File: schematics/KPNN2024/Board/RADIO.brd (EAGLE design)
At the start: 68.2 x 68.2 mm, 16 parts, among them J1 IPX-RADIO, J2 IPX-ANT

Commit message: ййййййййййййййййййййййййййййййййййй
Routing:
- net GND: track 161.2 -> 160.4 mm
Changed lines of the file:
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@@
 <?xml version="1.0" encoding="utf-8"?>
 <!DOCTYPE eagle SYSTEM "eagle.dtd">
-<eagle version="9.4.2">
+<eagle version="9.6.2">
 <drawing>
 <settings>
-<setting alwaysvectorfont="yes"/>
+<setting alwaysvectorfont="no"/>
 <setting verticaltext="up"/>
 </settings>
@@
 <contactref element="ROTATE2" pad="3"/>
 <contactref element="ROTATE1" pad="3"/>
-<wire x1="68.3698" y1="43.68434375" x2="68.477071875" y2="43.577071875" width="0.3" layer="1"/>
 <wire x1="64.921015625" y1="48.18434375" x2="64.985015625" y2="48.12034375" width="0.3" layer="1"/>
 <wire x1="64.985015625" y1="48.12034375" x2="64.985015625" y2="46.04934375" width="0.3" layer="1"/>
@@
 <wire x1="49.1" y1="48.18434375" x2="64.921015625" y2="48.18434375" width="0.5" layer="1"/>
 <wire x1="64.921015625" y1="48.18434375" x2="64.921015625" y2="43.68434375" width="0.5" layer="1"/>
-<wire x1="64.921015625" y1="43.68434375" x2="68.3698" y2="43.68434375" width="0.5" layer="1"/>
-<wire x1="68.477071875" y1="43.577071875" x2="68.636471875" y2="43.417671875" width="0.5" layer="1"/>
-<wire x1="68.636471875" y1="43.417671875" x2="68.636471875" y2="42.617671875" width="0.5" layer="1"/>
 <wire x1="68.636471875" y1="42.617671875" x2="68.636471875" y2="39.667671875" width="0.5" layer="1"/>
-<wire x1="68.636471875" y1="39.667671875" x2="68.15314375" y2="39.18434375" width="0.5" layer="1"/>
-<wire x1="68.15314375" y1="39.18434375" x2="64.921015625" y2="39.18434375" width="0.5" layer="1"/>
 <wire x1="24.741128125" y1="33.09638125" x2="24.741128125" y2="36.38238125" width="0.5" layer="1"/>
 <wire x1="24.734015625" y1="43.71034375" x2="23.034015625" y2="43.71034375" width="0.5" layer="1"/>
@@
 <wire x1="23.541128125" y1="36.38238125" x2="24.741128125" y2="36.38238125" width="0.5" layer="1"/>
 <wire x1="24.734015625" y1="43.71034375" x2="24.734015625" y2="46.66034375" width="0.5" layer="1"/>
-<wire x1="24.734015625" y1="46.66034375" x2="25.258015625" y2="47.18434375" width="0.5" layer="1"/>
-<wire x1="25.258015625" y1="47.18434375" x2="28.521015625" y2="47.18434375" width="0.5" layer="1"/>
-<wire x1="24.734015625" y1="43.71034375" x2="24.734015625" y2="43.18434375" width="0.5" layer="1"/>
-<wire x1="24.734015625" y1="43.18434375" x2="28.521015625" y2="43.18434375" width="0.5" layer="1"/>
 <wire x1="64.921015625" y1="48.18434375" x2="66.05634375" y2="48.18434375" width="0.5" layer="1"/>
 <wire x1="66.05634375" y1="48.18434375" x2="66.12034375" y2="48.12034375" width="0.5" layer="1"/>
@@
 <wire x1="69.23434375" y1="30.18434375" x2="64.921015625" y2="30.18434375" width="0.5" layer="1"/>
 <wire x1="61.8" y1="29.2" x2="62.8" y2="30.2" width="0.5" layer="1"/>
+<wire x1="68.636471875" y1="39.667671875" x2="68.15314375" y2="39.18434375" width="1" layer="1"/>
+<wire x1="68.15314375" y1="39.18434375" x2="64.921015625" y2="39.18434375" width="1" layer="1"/>
+<wire x1="68.636471875" y1="42.617671875" x2="67.5698" y2="43.68434375" width="1" layer="1"/>
+<wire x1="67.5698" y1="43.68434375" x2="64.921015625" y2="43.68434375" width="1" layer="1"/>
+<wire x1="24.734015625" y1="43.71034375" x2="25.260015625" y2="43.18434375" width="1" layer="1"/>
+<wire x1="25.260015625" y1="43.18434375" x2="28.521015625" y2="43.18434375" width="1" layer="1"/>
+<wire x1="24.734015625" y1="46.66034375" x2="25.258015625" y2="47.18434375" width="1" layer="1"/>
+<wire x1="25.258015625" y1="47.18434375" x2="28.521015625" y2="47.18434375" width="1" layer="1"/>
 </signal>
 <signal name="3V3">
@@
 <contactref element="J1" pad="3"/>
 <contactref element="XQ-02A" pad="RF-IN"/>
-<wire x1="67.111471875" y1="41.142671875" x2="64.9626875" y2="41.142671875" width="0.3" layer="1"/>
-<wire x1="64.921015625" y1="41.18434375" x2="64.9626875" y2="41.142671875" width="0.3" layer="1"/>
+<wire x1="67.111471875" y1="41.142671875" x2="64.9626875" y2="41.142671875" width="0.75" layer="1"/>
+<wire x1="64.9626875" y1="41.142671875" x2="64.921015625" y2="41.18434375" width="0.75" layer="1"/>
 </signal>
 <signal name="ANT_RADIO">
 <contactref element="J2" pad="3"/>
 <contactref element="XQ-02A" pad="ANT"/>
-<wire x1="26.259015625" y1="45.18534375" x2="28.520015625" y2="45.18534375" width="0.3" layer="1"/>
-<wire x1="28.520015625" y1="45.18534375" x2="28.521015625" y2="45.18434375" width="0.3" layer="1"/>
+<wire x1="26.259015625" y1="45.18534375" x2="28.520015625" y2="45.18534375" width="0.75" layer="1"/>
+<wire x1="28.520015625" y1="45.18534375" x2="28.521015625" y2="45.18434375" width="0.75" layer="1"/>
 </signal>
 <signal name="DIR_DRIVER">

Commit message: сдклвл платы а мботрен зз
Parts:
- moved NRF24LO1 0.37 mm to (50.0, 69.0)
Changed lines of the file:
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@@
 <attribute name="VALUE" x="24.5599875" y="48.321015625" size="1" layer="27" font="vector" ratio="15" align="center"/>
 </element>
-<element name="GPS-NEO7M" library="UNKNOWN-2024" package="GPS-NEO7M" value="GPS-NEO7M" x="50.900509375" y="64.0324625" smashed="yes" rot="MR270">
-<attribute name="NAME" x="61.5324625" y="77.099490625" size="1" layer="28" font="vector" ratio="15" rot="MR0"/>
-</element>
-<element name="NRF24LO1" library="UNKNOWN-2024" package="NRF24L01_ML01SP4" value="NRF24L01_ML01SP4" x="50.36748125" y="69.018953125" smashed="yes">
-<attribute name="NAME" x="41.36748125" y="77.118953125" size="1" layer="25" font="vector" ratio="15"/>
+<element name="GPS-NEO7M" library="UNKNOWN-2024" package="GPS-NEO7M" value="GPS-NEO7M" x="50.9" y="64" smashed="yes" rot="MR270">
+<attribute name="NAME" x="61.531953125" y="77.067028125" size="1" layer="28" font="vector" ratio="15" rot="MR0"/>
+</element>
+<element name="NRF24LO1" library="UNKNOWN-2024" package="NRF24L01_ML01SP4" value="NRF24L01_ML01SP4" x="50" y="69" smashed="yes">
+<attribute name="NAME" x="41" y="77.1" size="1" layer="25" font="vector" ratio="15"/>
 </element>
 <element name="XQ-02A" library="UNKNOWN-2024" package="XQ-02A" value="XQ-02A" x="46.721015625" y="37.18434375" smashed="yes" rot="R180">
@@
 <wire x1="29.714175" y1="47.18434375" x2="31.15" y2="48.62016875" width="0.5" layer="1"/>
 <wire x1="31.15" y1="56.4" x2="31.15" y2="48.62016875" width="0.5" layer="1"/>
-<wire x1="34.900509375" y1="60.2224625" x2="34.900509375" y2="60.150509375" width="0.5" layer="1"/>
+<wire x1="34.9" y1="60.19" x2="34.900509375" y2="60.150509375" width="0.5" layer="1"/>
 <wire x1="34.900509375" y1="60.150509375" x2="31.15" y2="56.4" width="0.5" layer="1"/>
-<wire x1="34.900509375" y1="60.2224625" x2="39.252" y2="64.573953125" width="0.5" layer="1"/>
-<wire x1="39.252" y1="64.573953125" x2="41.36748125" y2="64.573953125" width="0.5" layer="1"/>
-<wire x1="41.36748125" y1="64.573953125" x2="41.36748125" y2="55.9168625" width="0.5" layer="1"/>
-<wire x1="41.36748125" y1="55.9168625" x2="49.1" y2="48.18434375" width="0.5" layer="1"/>
+<wire x1="41" y1="56.28434375" x2="49.1" y2="48.18434375" width="0.5" layer="1"/>
 <wire x1="49.1" y1="48.18434375" x2="64.921015625" y2="48.18434375" width="0.5" layer="1"/>
 <wire x1="64.921015625" y1="48.18434375" x2="64.921015625" y2="43.68434375" width="0.5" layer="1"/>
@@
 <wire x1="24.734015625" y1="46.66034375" x2="25.258015625" y2="47.18434375" width="1" layer="1"/>
 <wire x1="25.258015625" y1="47.18434375" x2="28.521015625" y2="47.18434375" width="1" layer="1"/>
+<wire x1="41" y1="64.555" x2="41" y2="56.28434375" width="0.5" layer="1"/>
+<wire x1="34.9" y1="60.19" x2="39.265" y2="64.555" width="0.5" layer="1"/>
+<wire x1="39.265" y1="64.555" x2="41" y2="64.555" width="0.5" layer="1"/>
 </signal>
 <signal name="3V3">
@@
 <wire x1="31.08238125" y1="36.38238125" x2="37.7" y2="42.9" width="0.5" layer="1"/>
 <via x="37.7" y="42.9" extent="1-16" drill="0.35"/>
-<wire x1="41.36748125" y1="73.463953125" x2="37.736046875" y2="73.463953125" width="0.5" layer="1"/>
+<wire x1="41" y1="73.445" x2="37.736046875" y2="73.463953125" width="0.5" layer="1"/>
 <wire x1="37.736046875" y1="73.463953125" x2="37.7" y2="73.5" width="0.5" layer="1"/>
 <wire x1="37.7" y1="73.5" x2="37.7" y2="73.45" width="0.5" layer="1"/>
 <via x="37.7" y="73.45" extent="1-16" drill="0.35"/>
-<wire x1="41.36748125" y1="73.463953125" x2="43.476046875" y2="73.463953125" width="0.5" layer="1"/>
+<wire x1="41" y1="73.445" x2="43.476046875" y2="73.463953125" width="0.5" layer="1"/>
 <wire x1="43.476046875" y1="73.463953125" x2="49.7" y2="67.24" width="0.5" layer="1"/>
 <wire x1="71.16" y1="67.24" x2="71.2" y2="67.2" width="0.5" layer="1"/>
@@
 <wire x1="37.7" y1="42.9" x2="37.7" y2="67.8" width="0.5" layer="16"/>
 <wire x1="37.7" y1="67.8" x2="37.7" y2="73.45" width="0.5" layer="16"/>
-<wire x1="34.900509375" y1="67.8424625" x2="37.6575375" y2="67.8424625" width="0.5" layer="16"/>
-<wire x1="37.6575375" y1="67.8424625" x2="37.7" y2="67.8" width="0.5" layer="16"/>
+<wire x1="34.9" y1="67.81" x2="37.69" y2="67.81" width="0.5" layer="16"/>
+<wire x1="37.69" y1="67.81" x2="37.7" y2="67.8" width="0.5" layer="16"/>
 </signal>
 <signal name="5V">
@@
 <contactref element="NRF24LO1" pad="P$2"/>
 <wire x1="28.35" y1="72.16" x2="41.333528125" y2="72.16" width="0.3" layer="1"/>
-<wire x1="41.333528125" y1="72.16" x2="41.36748125" y2="72.193953125" width="0.3" layer="1"/>
+<wire x1="41.333528125" y1="72.16" x2="41" y2="72.175" width="0.3" layer="1"/>
 </signal>
 <signal name="CS_RADIO">
@@
 <contactref element="NRF24LO1" pad="P$3"/>
 <wire x1="25.65" y1="69.62" x2="25.65" y2="70.45" width="0.3" layer="1"/>
-<wire x1="25.65" y1="70.45" x2="26.123953125" y2="70.923953125" width="0.3" layer="1"/>
-<wire x1="26.123953125" y1="70.923953125" x2="33.4" y2="70.923953125" width="0.3" layer="1"/>
-<wire x1="33.4" y1="70.923953125" x2="41.36748125" y2="70.923953125" width="0.3" layer="1"/>
+<wire x1="25.65" y1="70.45" x2="26.105" y2="70.905" width="0.3" layer="1"/>
+<wire x1="26.105" y1="70.905" x2="41" y2="70.905" width="0.3" layer="1"/>
 </signal>
 <signal name="IRQ_RADIO">
 <contactref element="U$7" pad="3"/>
 <contactref element="NRF24LO1" pad="P$7"/>
-<wire x1="41.36748125" y1="65.843953125" x2="41.23090625" y2="65.980528125" width="0.3" layer="1"/>
-<wire x1="41.23090625" y1="65.980528125" x2="38.619471875" y2="65.980528125" width="0.3" layer="1"/>
-<wire x1="38.619471875" y1="65.980528125" x2="38.6" y2="66" width="0.3" layer="1"/>
 <via x="38.6" y="66" extent="1-16" drill="0.35"/>
 <wire x1="38.6" y1="75.10326875" x2="38.6" y2="66" width="0.3" layer="16"/>
@@
 <wire x1="38.6" y1="75.10326875" x2="36.30480625" y2="77.3984625" width="0.3" layer="16"/>
 <wire x1="33.3984625" y1="77.3984625" x2="31.2006375" y2="75.2006375" width="0.3" layer="16"/>
+<wire x1="38.6" y1="66" x2="38.775" y2="65.825" width="0.3" layer="1"/>
+<wire x1="38.775" y1="65.825" x2="41" y2="65.825" width="0.3" layer="1"/>
 </signal>
 <signal name="MOSI_RADIO">
 <contactref element="U$7" pad="4"/>
 <contactref element="NRF24LO1" pad="P$5"/>
-<wire x1="41.36748125" y1="68.383953125" x2="39.116046875" y2="68.383953125" width="0.3" layer="1"/>
-<wire x1="39.116046875" y1="68.383953125" x2="38.3" y2="69.2" width="0.3" layer="1"/>
-<wire x1="38.3" y1="69.2" x2="29" y2="69.2" width="0.3" layer="1"/>
+<wire x1="29" y1="69.2" x2="38.3" y2="69.2" width="0.3" layer="1"/>
 <wire x1="24.8071125" y1="68.1" x2="23.50355625" y2="66.79644375" width="0.3" layer="1"/>
 <wire x1="23.50355625" y1="66.79644375" x2="23.50355625" y2="64.89644375" width="0.3" layer="1"/>
@@
 <wire x1="29" y1="69.2" x2="27.9" y2="68.1" width="0.3" layer="1"/>
 <wire x1="27.9" y1="68.1" x2="24.8071125" y2="68.1" width="0.3" layer="1"/>
+<wire x1="39.135" y1="68.365" x2="41" y2="68.365" width="0.3" layer="1"/>
+<wire x1="38.3" y1="69.2" x2="39.135" y2="68.365" width="0.3" layer="1"/>
 </signal>
 <signal name="MISO_RADIO">
@@
 <wire x1="30.35" y1="62.3" x2="30.05" y2="62" width="0.3" layer="1"/>
 <wire x1="28.35" y1="62" x2="30.05" y2="62" width="0.3" layer="1"/>
-<wire x1="41.36748125" y1="67.113953125" x2="41.253528125" y2="67" width="0.3" layer="1"/>
-<wire x1="41.253528125" y1="67" x2="39.4" y2="67" width="0.3" layer="1"/>
 <via x="39.4" y="67" extent="1-16" drill="0.35"/>
 <wire x1="39.4" y1="76.6" x2="39.4" y2="67" width="0.3" layer="16"/>
@@
 <wire x1="39.4" y1="76.6" x2="37.6015375" y2="78.3984625" width="0.3" layer="16"/>
 <wire x1="33.3984625" y1="78.3984625" x2="30.3" y2="75.3" width="0.3" layer="16"/>
+<wire x1="39.4" y1="67" x2="40.905" y2="67" width="0.3" layer="1"/>
+<wire x1="40.905" y1="67" x2="41" y2="67.095" width="0.3" layer="1"/>
 </signal>
 <signal name="SCK_RADIO">
@@
 <wire x1="23.84" y1="59.46" x2="23" y2="60.3" width="0.3" layer="1"/>
 <wire x1="23" y1="67" x2="23" y2="60.3" width="0.3" layer="1"/>
-<wire x1="41.36748125" y1="69.653953125" x2="39.06748125" y2="69.653953125" width="0.3" layer="1"/>
-<wire x1="39.06748125" y1="69.653953125" x2="38.66748125" y2="70.053953125" width="0.3" layer="1"/>
-<wire x1="38.66748125" y1="70.053953125" x2="29.053953125" y2="70.053953125" width="0.3" layer="1"/>
+<wire x1="29.053953125" y1="70.053953125" x2="38.66748125" y2="70.053953125" width="0.3" layer="1"/>
 <wire x1="29.053953125" y1="70.053953125" x2="27.6" y2="68.6" width="0.3" layer="1"/>
 <wire x1="27.6" y1="68.6" x2="24.6" y2="68.6" width="0.3" layer="1"/>
 <wire x1="24.6" y1="68.6" x2="23" y2="67" width="0.3" layer="1"/>
+<wire x1="39.086434375" y1="69.635" x2="41" y2="69.635" width="0.3" layer="1"/>
+<wire x1="38.66748125" y1="70.053953125" x2="39.086434375" y2="69.635" width="0.3" layer="1"/>
 </signal>
 <signal name="TX2_GPS">
 <contactref element="U$7" pad="7"/>
 <contactref element="GPS-NEO7M" pad="P$3"/>
-<wire x1="33.169021875" y1="61.030975" x2="34.900509375" y2="62.7624625" width="0.3" layer="1"/>
+<wire x1="33.169021875" y1="61.030975" x2="34.9" y2="62.73" width="0.3" layer="1"/>
 <wire x1="28.35" y1="56.92" x2="30.32" y2="56.92" width="0.3" layer="1"/>
 <wire x1="33.169021875" y1="59.769021875" x2="33.169021875" y2="61.030975" width="0.3" layer="1"/>
@@
 <wire x1="25.65" y1="54.38" x2="25.65" y2="57.00765625" width="0.3" layer="1"/>
 <wire x1="25.65" y1="57.00765625" x2="26.87474375" y2="58.2324" width="0.3" layer="1"/>
-<wire x1="27.830446875" y1="58.2324" x2="34.900509375" y2="65.3024625" width="0.3" layer="1"/>
+<wire x1="27.830446875" y1="58.2324" x2="34.9" y2="65.27" width="0.3" layer="1"/>
 </signal>
 <signal name="SW_WMP">

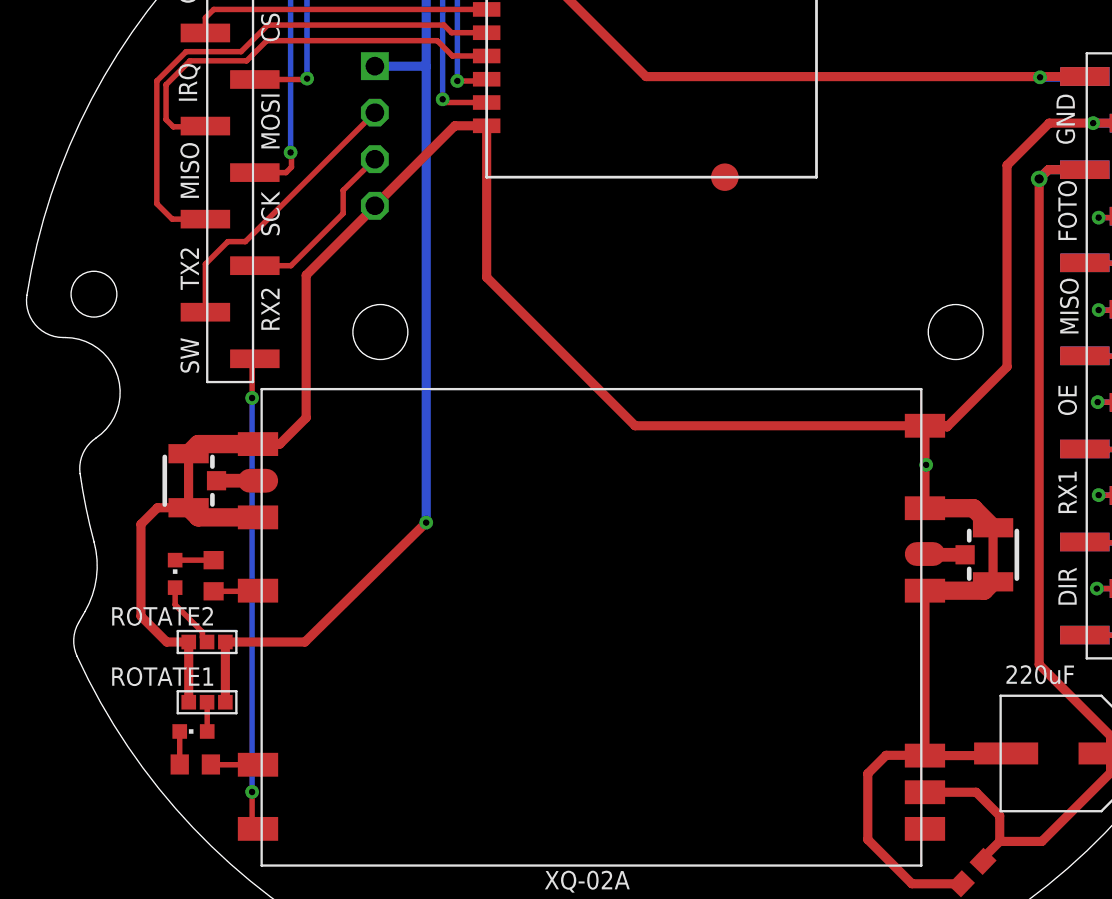
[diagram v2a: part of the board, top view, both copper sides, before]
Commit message: поправила платы
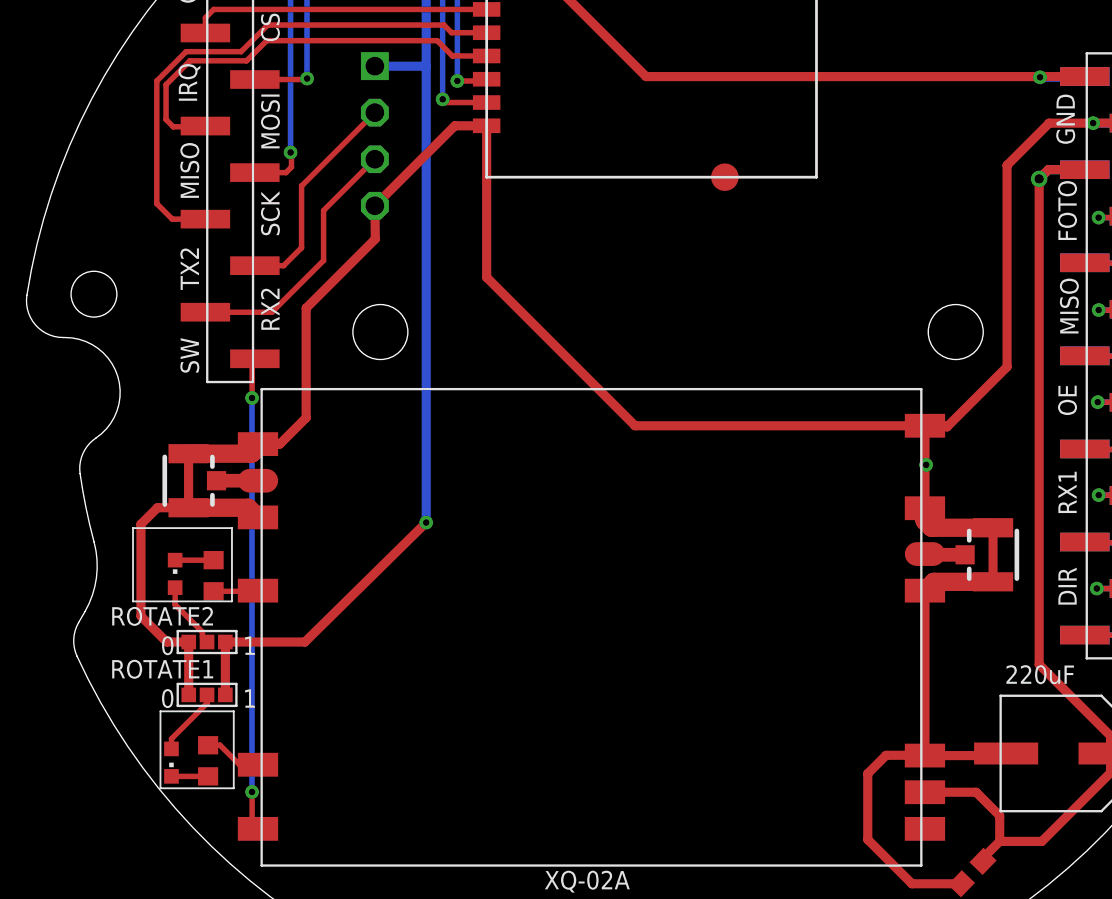
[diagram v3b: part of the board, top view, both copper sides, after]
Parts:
- moved LED1 2.08 mm to (23.8, 29.8), turned to 180 degrees
- moved R1 0.73 mm to (25.8, 29.9), turned to 270 degrees
- moved ROTATE1 0.40 mm to (25.7, 33.5)
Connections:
- net RX2_GPS: now also GPS-NEO7M.P$3; no longer GPS-NEO7M.P$2
- net TX2_GPS: now also GPS-NEO7M.P$2; no longer GPS-NEO7M.P$3
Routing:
- net N$3: track 1.60 -> 4.06 mm
- net TX2_GPS: track 9.69 -> 12.0 mm
- net RX2_GPS: track 15.3 -> 14.3 mm
- net N$6: track 2.58 -> 3.16 mm
